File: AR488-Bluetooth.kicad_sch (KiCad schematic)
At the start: 24 parts, among them J1 112-024-213R001, J3 HC-05, P1 Digital, P10 CONN_01X01, P11 CONN_01X01, P12 CONN_01X01, P13 CONN_01X01, P2 Power, P3 Analog, P4 Analog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

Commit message: Correct the design and add the battery circuit. No Gerber is generated
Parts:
- added BT1: Battery, Connector_PinHeader_2.54mm:PinHeader_1x02_P2.54mm_Vertical, symbol Device:Battery
- added C1, C2, C3: 10u, Capacitor_SMD:C_0402_1005Metric_Pad0.74x0.62mm_HandSolder, symbol Device:C
- added C4, C5: 0.1u, Capacitor_SMD:C_0603_1608Metric_Pad1.08x0.95mm_HandSolder, symbol Device:C
- added D2: BAT LOW, LED_THT:LED_D3.0mm, symbol Device:LED
- added JP5: CE_SEL, Jumper:SolderJumper-3_P1.3mm_Open_Pad1.0x1.5mm_NumberLabels, symbol Jumper:SolderJumper_3_Open
- added L1: 4.7u, Inductor_SMD:L_0805_2012Metric_Pad1.15x1.40mm_HandSolder, symbol Device:L
- added R2: 1k, Resistor_SMD:R_0603_1608Metric_Pad0.98x0.95mm_HandSolder, symbol Device:R
- added RV1: 5M, Potentiometer_THT:Potentiometer_Bourns_3299W_Vertical, symbol Device:R_Potentiometer_Small
- added SW1: SW_SPDT, Socket_Arduino_Mega:STSSS9121, symbol Switch:SW_SPDT
- added TP1: TestPoint, TestPoint:TestPoint_Keystone_5015_Micro-Minature, symbol Connector:TestPoint
- added U4: XC9141B50CMR-G, Package_TO_SOT_SMD:SOT-23-5_HandSoldering, symbol AR488:XC9141B50CMR-G
- added U5: MCP65R41T-1202E/CHY, Package_TO_SOT_SMD:SOT-23-6_Handsoldering, symbol AR488:MCP65R41T-1202E/CHY
- R1: footprint Resistor_THT:R_Axial_DIN0207_L6.3mm_D2.5mm_P10.16mm_Horizontal -> Resistor_SMD:R_0603_1608Metric_Pad0.98x0.95mm_HandSolder
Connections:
- net +5V: now also C2.1, C3.1, C4.1, C5.1, U4.4 (Vout)
- net GND: now also BT1.2 (-), C1.2, C2.2, C3.2, C4.2, C5.2, RV1.3, U4.2 (GND), U5.2 (VSS)
- new net: D2.2 (A), R2.2
- new net +BATT: C1.1, JP5.1 (A), L1.1, R2.1, RV1.1, SW1.3 (C), U4.3 (BAT), U5.6 (VDD)
- new net BAT_IN: BT1.1 (+), SW1.2 (B)
- new net CE: JP5.2 (C), U4.1 (CE)
- new net CE_OUT: D2.1 (K), JP5.3 (B), U5.1 (OUT)
- new net IN+: RV1.2, TP1.1, U5.3 (+IN)
- new net IN-: U5.4 (-IN), U5.5 (Vref)
- new net Lx: L1.2, U4.5 (Lx)
- no-connect marks 13 -> 14
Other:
- note added: "9V battery Regulator & Indicator"
- moved on the sheet: J1

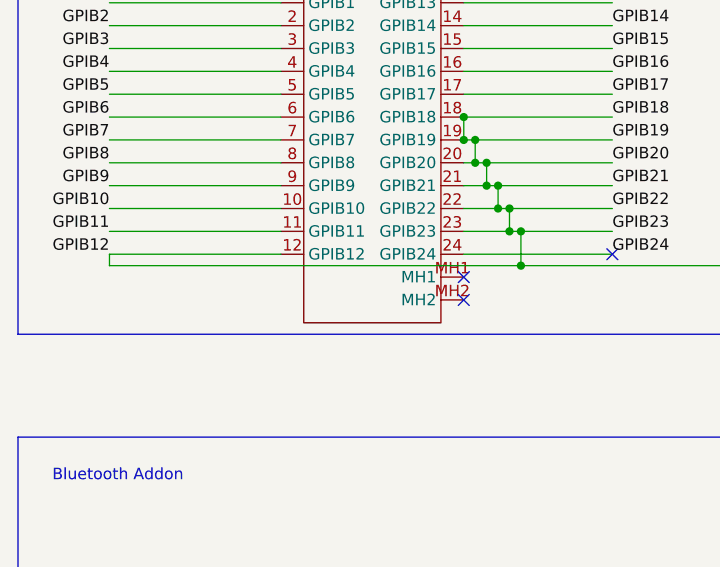
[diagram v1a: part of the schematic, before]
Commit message: Update the images and connect shield to GND
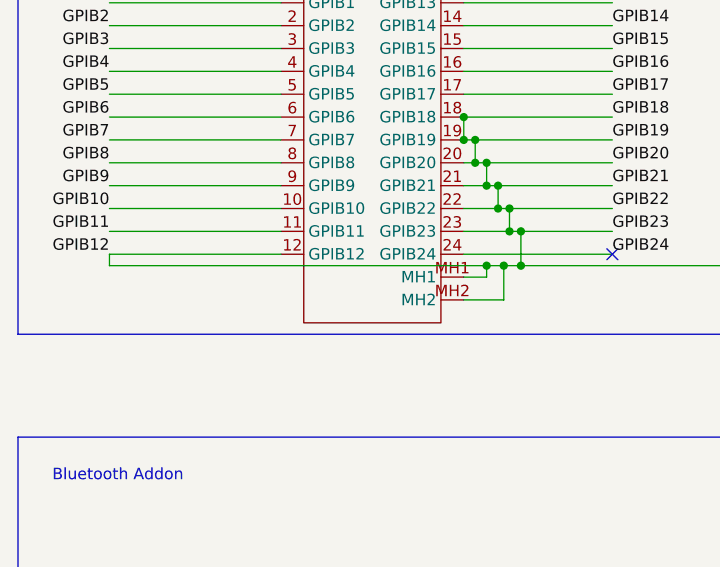
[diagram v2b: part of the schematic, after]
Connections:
- net GND: now also J1.MH1, J1.MH2
- no-connect marks 14 -> 12
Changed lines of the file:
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@@
   (junction (at 234.95 49.53) (diameter 1.016) (color 0 0 0 0)
   )
+  (junction (at 79.375 120.65) (diameter 0) (color 0 0 0 0)
+  )
   (junction (at 80.01 114.3) (diameter 0) (color 0 0 0 0)
   )
@@
   )
   (junction (at 134.62 95.25) (diameter 0) (color 0 0 0 0)
+  )
+  (junction (at 77.47 120.65) (diameter 0) (color 0 0 0 0)
   )
   (junction (at 77.47 109.22) (diameter 0) (color 0 0 0 0)
@@
   (no_connect (at 271.78 21.59))
   (no_connect (at 281.94 21.59))
-  (no_connect (at 74.93 121.92))
-  (no_connect (at 74.93 124.46))
   (no_connect (at 276.86 21.59))
   (no_connect (at 279.4 21.59))
@@
     (stroke (width 0) (type solid) (color 0 0 0 0))
   )
+  (wire (pts (xy 74.93 121.92) (xy 77.47 121.92))
+    (stroke (width 0) (type default) (color 0 0 0 0))
+  )
   (wire (pts (xy 234.95 36.83) (xy 234.95 30.48))
     (stroke (width 0) (type solid) (color 0 0 0 0))
@@
     (stroke (width 0) (type default) (color 0 0 0 0))
   )
-  (wire (pts (xy 35.56 120.65) (xy 81.28 120.65))
+  (wire (pts (xy 35.56 120.65) (xy 77.47 120.65))
     (stroke (width 0) (type default) (color 0 0 0 0))
   )
@@
     (stroke (width 0) (type solid) (color 0 0 0 0))
   )
+  (wire (pts (xy 77.47 120.65) (xy 79.375 120.65))
+    (stroke (width 0) (type default) (color 0 0 0 0))
+  )
   (wire (pts (xy 264.16 67.31) (xy 257.81 67.31))
     (stroke (width 0) (type solid) (color 0 0 0 0))
@@
     (stroke (width 0) (type default) (color 0 0 0 0))
   )
+  (wire (pts (xy 79.375 120.65) (xy 81.28 120.65))
+    (stroke (width 0) (type default) (color 0 0 0 0))
+  )
   (wire (pts (xy 260.35 36.83) (xy 257.81 36.83))
     (stroke (width 0) (type solid) (color 0 0 0 0))
@@
     (stroke (width 0) (type default) (color 0 0 0 0))
   )
+  (wire (pts (xy 77.47 121.92) (xy 77.47 120.65))
+    (stroke (width 0) (type default) (color 0 0 0 0))
+  )
   (wire (pts (xy 118.11 171.45) (xy 128.27 171.45))
     (stroke (width 0) (type default) (color 0 0 0 0))
@@
   )
   (wire (pts (xy 153.67 95.25) (xy 156.21 95.25))
+    (stroke (width 0) (type default) (color 0 0 0 0))
+  )
+  (wire (pts (xy 79.375 124.46) (xy 79.375 120.65))
     (stroke (width 0) (type default) (color 0 0 0 0))
   )
@@
     (stroke (width 0) (type dash) (color 0 0 0 0))
   )
+  (wire (pts (xy 74.93 124.46) (xy 79.375 124.46))
+    (stroke (width 0) (type default) (color 0 0 0 0))
+  )
   (wire (pts (xy 156.21 95.25) (xy 161.29 95.25))

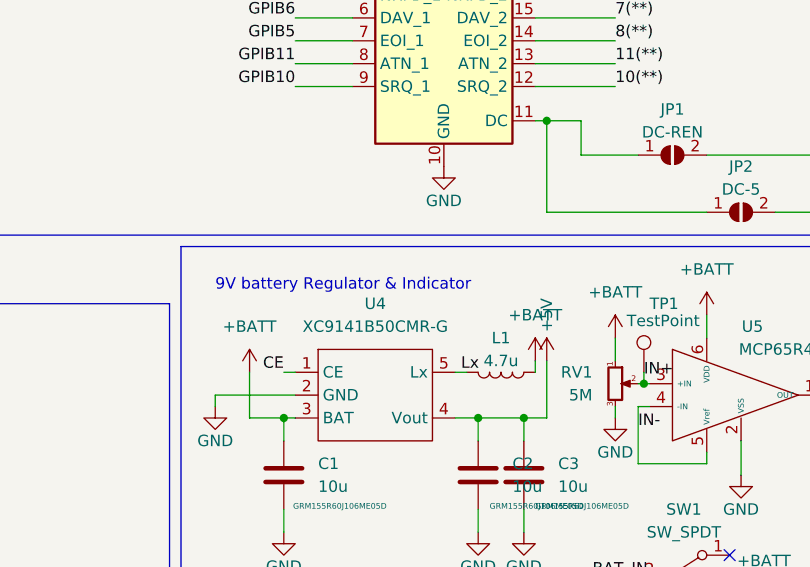
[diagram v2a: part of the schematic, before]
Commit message: Update typo in the schematic
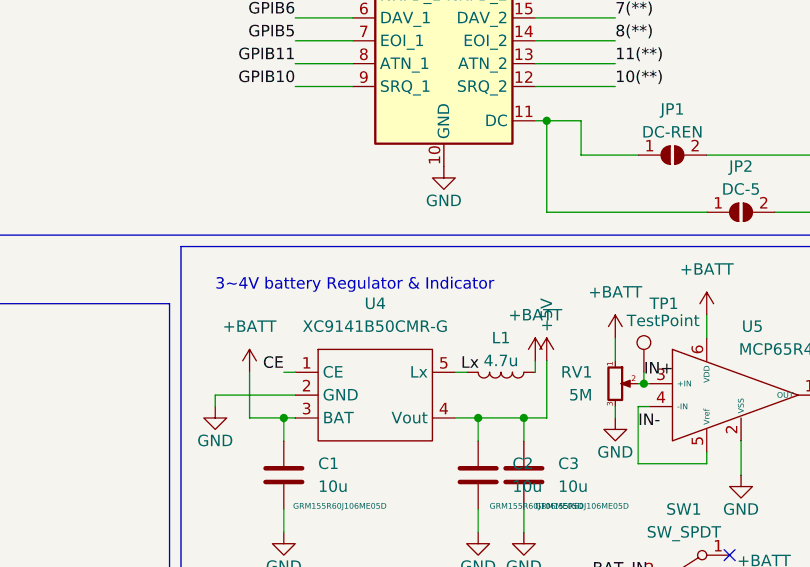
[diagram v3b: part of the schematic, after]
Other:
- note added: "3~4V battery Regulator & Indicator"
- note removed: "9V battery Regulator & Indicator"
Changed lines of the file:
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@@
     (effects (font (size 1.27 1.27)) (justify left bottom))
   )
-  (text "9V battery Regulator & Indicator" (at 127 81.28 0)
+  (text "3~4V battery Regulator & Indicator" (at 127 81.28 0)
     (effects (font (size 1.27 1.27)) (justify left bottom))
   )
